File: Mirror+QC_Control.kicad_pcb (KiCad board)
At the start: 2 copper layers, 107 x 82 mm, 71 parts, among them J2 Screw_Terminal_01x04, J3 Screw_Terminal_01x06, J4 FSM DRIVER, U1 LT1012, U10 LT1012, U11 LT1012, U2 LM4040DBZ-2.0, U3 LT1012, U5 LT1012, U6 LT1012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

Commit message: final changes to board with nice layout
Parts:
- U1, U10, U11, U3, U5, U6: footprint Package_SO:SOIC-8_3.9x4.9mm_P1.27mm -> Package_DIP:DIP-8_W7.62mm
- moved U5 10.6 mm to (78.2, 90.7)
- moved R1 9.16 mm to (77.7, 38.0)
- moved R7 9.04 mm to (78.0, 64.0)
- moved U1 8.60 mm to (81.7, 65.2)
- moved U10 8.22 mm to (81.2, 39.7)
- moved R12 6.67 mm to (74.7, 93.5)
- moved U3 5.79 mm to (102.2, 66.7)
- moved C16 5.59 mm to (81.7, 102.5)
- moved R4 5.59 mm to (82.0, 100.8)
- moved R8 5.56 mm to (77.8, 66.0)
- moved C10 5.48 mm to (110.5, 43.5), turned to 90 degrees
- moved U6 5.31 mm to (101.2, 91.7)
- moved R3 5.25 mm to (77.7, 40.0)
- moved C14 4.68 mm to (76.0, 100.0), turned to -90 degrees
- moved U11 4.45 mm to (100.2, 41.7)
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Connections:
- J2 pad 1: +15V -> GND
- J2 pad 2: -15V -> +15V
- J2 pad 3: +5V -> -15V
- J2 pad 4: GND -> +5V
- J3 pad 1: /x+ -> GND
- J3 pad 2: /y+ -> +15V
- J3 pad 3: /sum -> -15V
- J3 pad 4: +15V -> /x+
- J3 pad 5: -15V -> /y+
- J3 pad 6: GND -> /sum
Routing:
- net GND: track 444.9 -> 128.3 mm, vias 20 -> 2
- net /sum: track 58.5 -> 39.1 mm, vias 0 -> 2
- net +5V: track 139.4 -> 121.6 mm
- net /y+: track 41.4 -> 24.4 mm, vias 2 -> 4
- net /y_stage2: track 69.9 -> 53.0 mm
- net +15V: track 243.0 -> 229.9 mm, vias 9 -> 4
- net /EN: track 69.7 -> 59.7 mm, vias 2 -> 4
- net /sum_stage1: track 19.2 -> 28.5 mm
- net /SYNC: track 61.1 -> 53.9 mm
- net /sum_stage2: track 73.2 -> 80.2 mm
- net /FCLK_Y: track 39.7 -> 32.9 mm
- net Net-(U6--): track 19.6 -> 13.1 mm, vias 2 -> 0
- net /FCLK_X: track 38.9 -> 34.0 mm
- net Net-(U5--): track 17.6 -> 13.4 mm, vias 2 -> 0
- net Net-(U10--): track 14.1 -> 18.2 mm, vias 2 -> 1
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- added copper zone on F.Cu, net GND
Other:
- outline, holes or cut-outs redrawn

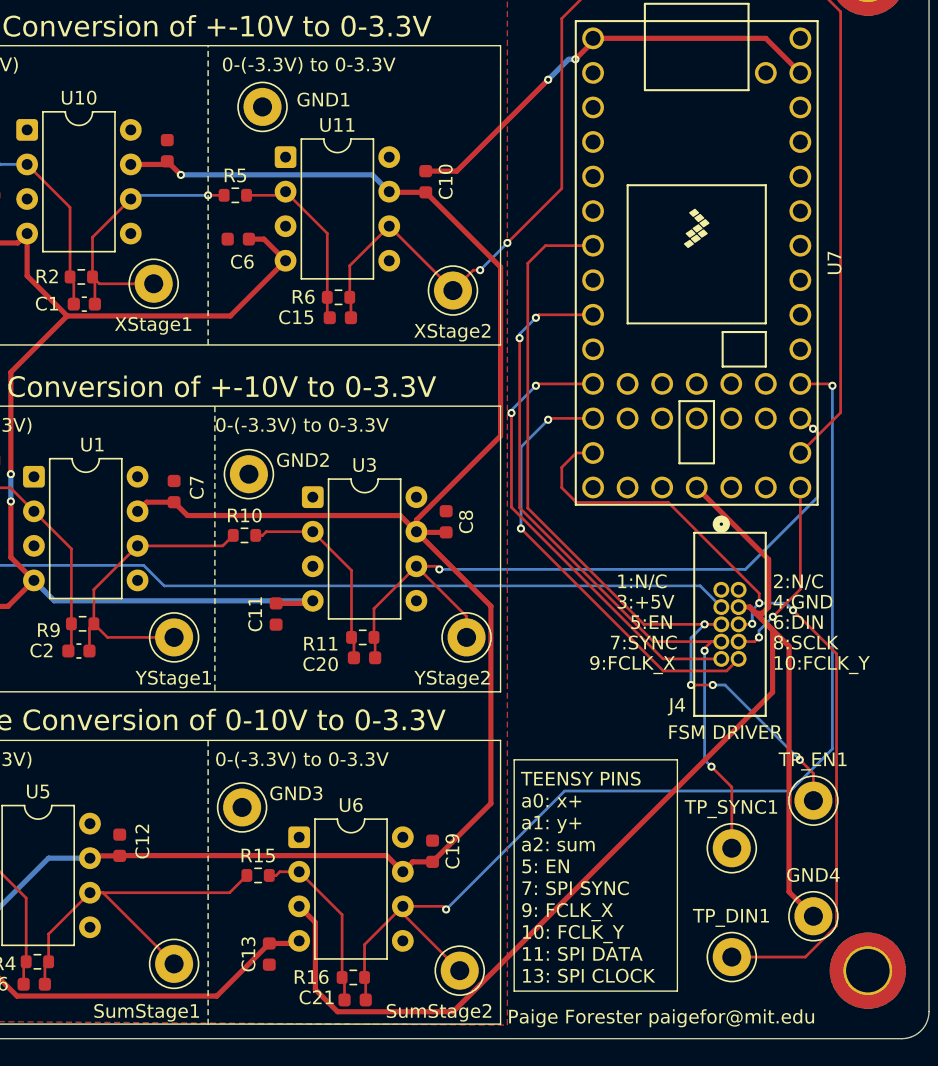
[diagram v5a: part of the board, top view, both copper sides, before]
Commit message: adding all LCSC part numbers
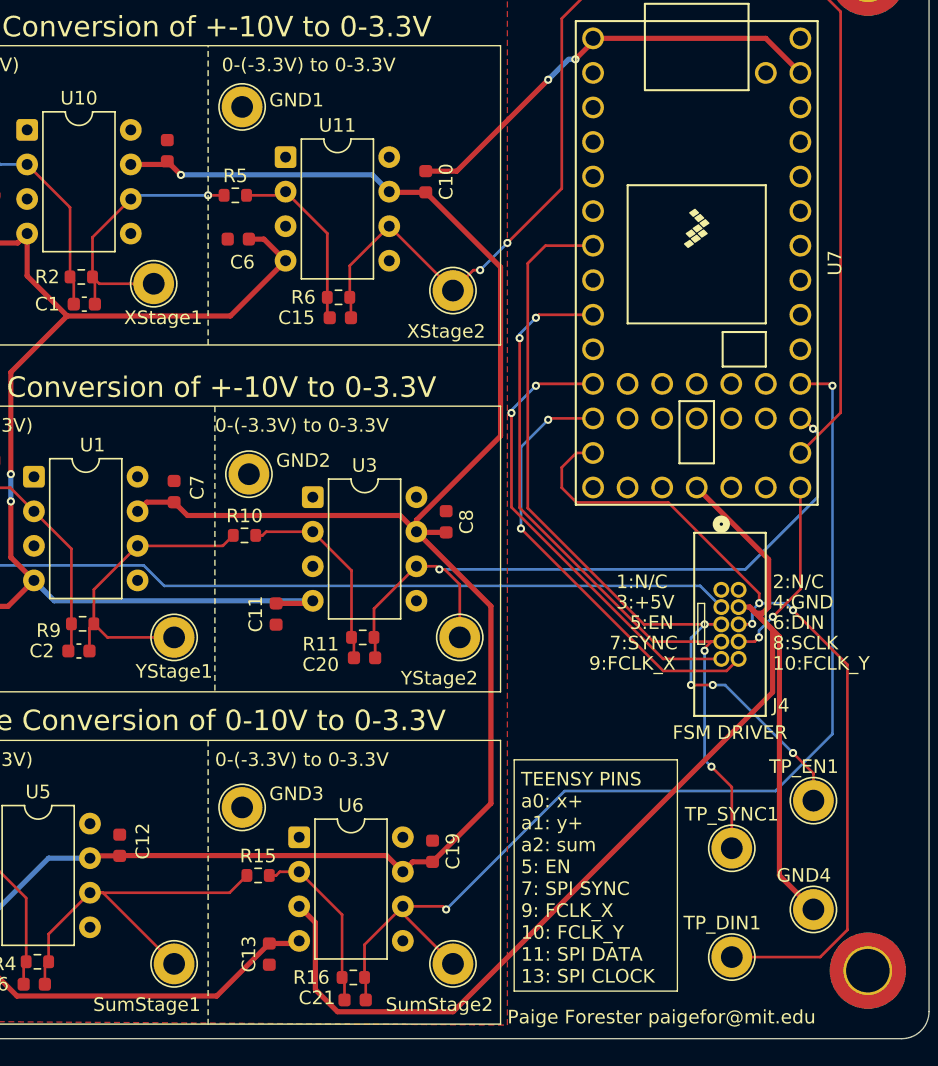
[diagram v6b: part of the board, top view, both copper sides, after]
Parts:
- GND1, GND2, GND3, GND4, SumStage1, SumStage2, TP_DIN1, TP_EN1, TP_SYNC1, XStage1, XStage2, YStage1, YStage2: footprint TestPoint:TestPoint_Loop_D3.50mm_Drill1.4mm_Beaded -> TestPoint:TestPoint_Loop_D2.60mm_Drill1.6mm_Beaded
- R13, R14: value 1300 -> 1200
- moved GND1 1.50 mm to (97.0, 38.0)
- moved SumStage2 0.71 mm to (112.5, 101.0)
- moved GND4 0.50 mm to (139.0, 97.0)
- moved YStage2 0.50 mm to (113.0, 77.0)
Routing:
- net /sum_stage2: track 80.2 -> 78.9 mm
- net /DIN: track 61.3 -> 62.6 mm
- net /y_stage2: track 53.0 -> 52.1 mm
- net GND: track 128.3 -> 127.8 mm

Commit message: added OpAmp drop in parts and oriented properly
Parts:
- U1, U10, U11, U3, U5, U6: footprint Package_DIP:DIP-8_W7.62mm -> DIP THING:CONN8_1-2199298-2_TEC
- moved C12 2.12 mm to (89.5, 90.8)
- moved U5 0.79 mm to (78.4, 89.9), turned to -90 degrees
- moved U10 0.36 mm to (81.5, 39.5), turned to -90 degrees
- turned U1 to -90 degrees
- turned U11 to -90 degrees
- turned U3 to -90 degrees
- turned U6 to -90 degrees
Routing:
- net -15V: track 217.1 -> 217.9 mm
- net /x_stage1: track 21.1 -> 21.4 mm, vias 1 -> 2
- net Net-(U10--): vias 1 -> 0
